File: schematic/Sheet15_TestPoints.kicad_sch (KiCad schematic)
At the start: 16 parts

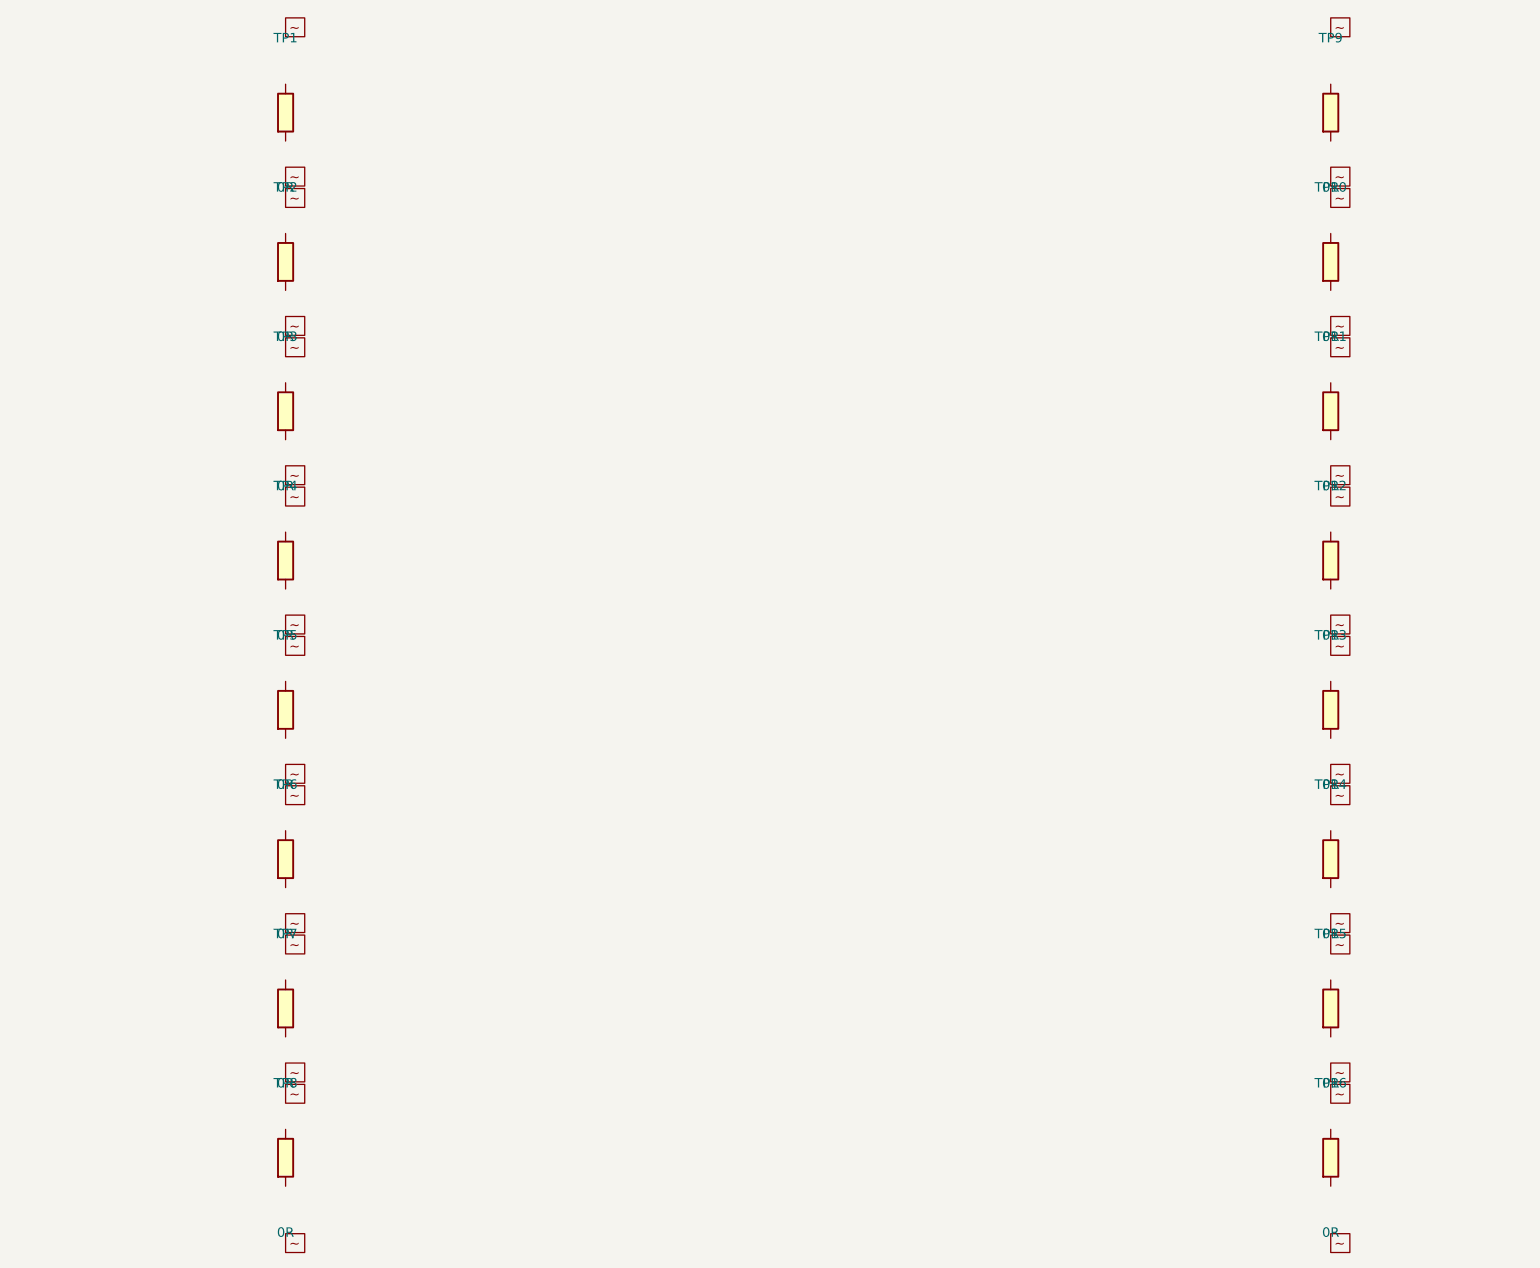
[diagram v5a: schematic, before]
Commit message: feat: connect ALL passive components and fix clock routing
- Added PASSIVE_TOPOLOGY dict mapping 139 passives to their nets
- Passive pin endpoints now get global_labels (was 0 connected, now 138)
- R38 intentionally GND-GND (RECAL_EN pull-down)
- Fixed LMK clock output mapping: CLKout0→ADC_CLK_P, CLKout2→FPGA_REFCLK_P, etc.
- Fixed TPS7H5001-SP SYNC pin collision with LMX_SYNC
- Total connections: 867 pins (up from 641)
- Cross-sheet nets: 52
- Power rails: VIN(33), +3V3(98), GND(228) all with decoupling
- JESD204C: U1↔U2 on 4 lanes ✓
- SPI: U1↔U2↔U3↔U4 ✓
- Clock: LMK→ADC (CLK+SYSREF), LMK→FPGA (REF+SPW) ✓
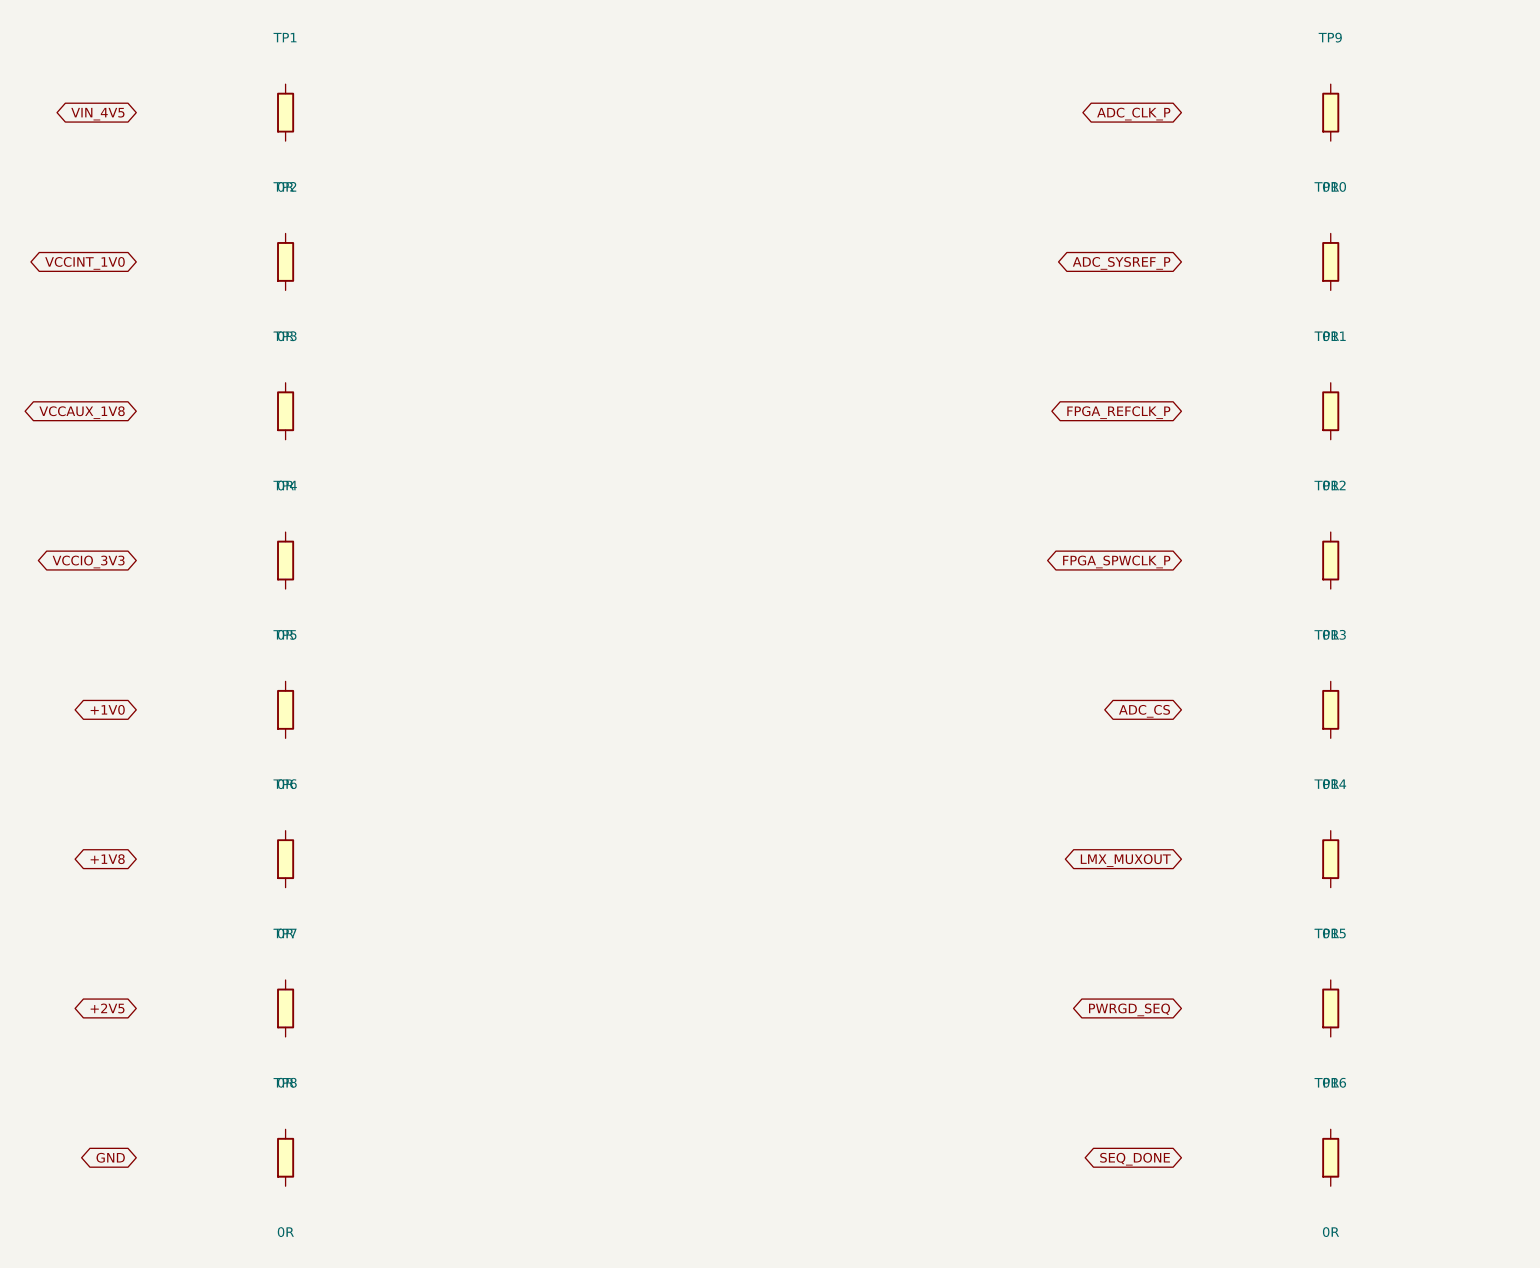
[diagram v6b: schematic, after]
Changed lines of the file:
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@@
     (pin "1")
     (pin "2")
-  )    (symbol (lib_id "Device:R") (at 60 60 0) (unit 1)
+  )  (global_label "VIN_4V5" (shape bidirectional) (at 40 40 180) (effects (font (size 1.27 1.27)) (justify right)))  (symbol (lib_id "Device:R") (at 60 60 0) (unit 1)
     (in_bom yes) (on_board yes)
     (property "Reference" "TP2" (at 60 50 0) (effects (font (size 1.27 1.27))))
@@
     (pin "1")
     (pin "2")
-  )    (symbol (lib_id "Device:R") (at 60 80 0) (unit 1)
+  )  (global_label "VCCINT_1V0" (shape bidirectional) (at 40 60 180) (effects (font (size 1.27 1.27)) (justify right)))  (symbol (lib_id "Device:R") (at 60 80 0) (unit 1)
     (in_bom yes) (on_board yes)
     (property "Reference" "TP3" (at 60 70 0) (effects (font (size 1.27 1.27))))
@@
     (pin "1")
     (pin "2")
-  )    (symbol (lib_id "Device:R") (at 60 100 0) (unit 1)
+  )  (global_label "VCCAUX_1V8" (shape bidirectional) (at 40 80 180) (effects (font (size 1.27 1.27)) (justify right)))  (symbol (lib_id "Device:R") (at 60 100 0) (unit 1)
     (in_bom yes) (on_board yes)
     (property "Reference" "TP4" (at 60 90 0) (effects (font (size 1.27 1.27))))
@@
     (pin "1")
     (pin "2")
-  )    (symbol (lib_id "Device:R") (at 60 120 0) (unit 1)
+  )  (global_label "VCCIO_3V3" (shape bidirectional) (at 40 100 180) (effects (font (size 1.27 1.27)) (justify right)))  (symbol (lib_id "Device:R") (at 60 120 0) (unit 1)
     (in_bom yes) (on_board yes)
     (property "Reference" "TP5" (at 60 110 0) (effects (font (size 1.27 1.27))))
@@
     (pin "1")
     (pin "2")
-  )    (symbol (lib_id "Device:R") (at 60 140 0) (unit 1)
+  )  (global_label "+1V0" (shape bidirectional) (at 40 120 180) (effects (font (size 1.27 1.27)) (justify right)))  (symbol (lib_id "Device:R") (at 60 140 0) (unit 1)
     (in_bom yes) (on_board yes)
     (property "Reference" "TP6" (at 60 130 0) (effects (font (size 1.27 1.27))))
@@
     (pin "1")
     (pin "2")
-  )    (symbol (lib_id "Device:R") (at 60 160 0) (unit 1)
+  )  (global_label "+1V8" (shape bidirectional) (at 40 140 180) (effects (font (size 1.27 1.27)) (justify right)))  (symbol (lib_id "Device:R") (at 60 160 0) (unit 1)
     (in_bom yes) (on_board yes)
     (property "Reference" "TP7" (at 60 150 0) (effects (font (size 1.27 1.27))))
@@
     (pin "1")
     (pin "2")
-  )    (symbol (lib_id "Device:R") (at 60 180 0) (unit 1)
+  )  (global_label "+2V5" (shape bidirectional) (at 40 160 180) (effects (font (size 1.27 1.27)) (justify right)))  (symbol (lib_id "Device:R") (at 60 180 0) (unit 1)
     (in_bom yes) (on_board yes)
     (property "Reference" "TP8" (at 60 170 0) (effects (font (size 1.27 1.27))))
@@
     (pin "1")
     (pin "2")
-  )    (symbol (lib_id "Device:R") (at 200 40 0) (unit 1)
+  )  (global_label "GND" (shape bidirectional) (at 40 180 180) (effects (font (size 1.27 1.27)) (justify right)))  (symbol (lib_id "Device:R") (at 200 40 0) (unit 1)
     (in_bom yes) (on_board yes)
     (property "Reference" "TP9" (at 200 30 0) (effects (font (size 1.27 1.27))))
@@
     (pin "1")
     (pin "2")
-  )    (symbol (lib_id "Device:R") (at 200 60 0) (unit 1)
+  )  (global_label "ADC_CLK_P" (shape bidirectional) (at 180 40 180) (effects (font (size 1.27 1.27)) (justify right)))  (symbol (lib_id "Device:R") (at 200 60 0) (unit 1)
     (in_bom yes) (on_board yes)
     (property "Reference" "TP10" (at 200 50 0) (effects (font (size 1.27 1.27))))
@@
     (pin "1")
     (pin "2")
-  )    (symbol (lib_id "Device:R") (at 200 80 0) (unit 1)
+  )  (global_label "ADC_SYSREF_P" (shape bidirectional) (at 180 60 180) (effects (font (size 1.27 1.27)) (justify right)))  (symbol (lib_id "Device:R") (at 200 80 0) (unit 1)
     (in_bom yes) (on_board yes)
     (property "Reference" "TP11" (at 200 70 0) (effects (font (size 1.27 1.27))))
@@
     (pin "1")
     (pin "2")
-  )    (symbol (lib_id "Device:R") (at 200 100 0) (unit 1)
+  )  (global_label "FPGA_REFCLK_P" (shape bidirectional) (at 180 80 180) (effects (font (size 1.27 1.27)) (justify right)))  (symbol (lib_id "Device:R") (at 200 100 0) (unit 1)
     (in_bom yes) (on_board yes)
     (property "Reference" "TP12" (at 200 90 0) (effects (font (size 1.27 1.27))))
@@
     (pin "1")
     (pin "2")
-  )    (symbol (lib_id "Device:R") (at 200 120 0) (unit 1)
+  )  (global_label "FPGA_SPWCLK_P" (shape bidirectional) (at 180 100 180) (effects (font (size 1.27 1.27)) (justify right)))  (symbol (lib_id "Device:R") (at 200 120 0) (unit 1)
     (in_bom yes) (on_board yes)
     (property "Reference" "TP13" (at 200 110 0) (effects (font (size 1.27 1.27))))
@@
     (pin "1")
     (pin "2")
-  )    (symbol (lib_id "Device:R") (at 200 140 0) (unit 1)
+  )  (global_label "ADC_CS" (shape bidirectional) (at 180 120 180) (effects (font (size 1.27 1.27)) (justify right)))  (symbol (lib_id "Device:R") (at 200 140 0) (unit 1)
     (in_bom yes) (on_board yes)
     (property "Reference" "TP14" (at 200 130 0) (effects (font (size 1.27 1.27))))
@@
     (pin "1")
     (pin "2")
-  )    (symbol (lib_id "Device:R") (at 200 160 0) (unit 1)
+  )  (global_label "LMX_MUXOUT" (shape bidirectional) (at 180 140 180) (effects (font (size 1.27 1.27)) (justify right)))  (symbol (lib_id "Device:R") (at 200 160 0) (unit 1)
     (in_bom yes) (on_board yes)
     (property "Reference" "TP15" (at 200 150 0) (effects (font (size 1.27 1.27))))
@@
     (pin "1")
     (pin "2")
-  )    (symbol (lib_id "Device:R") (at 200 180 0) (unit 1)
+  )  (global_label "PWRGD_SEQ" (shape bidirectional) (at 180 160 180) (effects (font (size 1.27 1.27)) (justify right)))  (symbol (lib_id "Device:R") (at 200 180 0) (unit 1)
     (in_bom yes) (on_board yes)
     (property "Reference" "TP16" (at 200 170 0) (effects (font (size 1.27 1.27))))
@@
     (pin "1")
     (pin "2")
-  )
-  (global_label "~" (at 60.0000 28.5700 0) (effects (font (size 1.27 1.27))))
-  (global_label "~" (at 60.0000 51.4300 0) (effects (font (size 1.27 1.27))))
-  (global_label "~" (at 60.0000 48.5700 0) (effects (font (size 1.27 1.27))))
-  (global_label "~" (at 60.0000 71.4300 0) (effects (font (size 1.27 1.27))))
-  (global_label "~" (at 60.0000 68.5700 0) (effects (font (size 1.27 1.27))))
-  (global_label "~" (at 60.0000 91.4300 0) (effects (font (size 1.27 1.27))))
-  (global_label "~" (at 60.0000 88.5700 0) (effects (font (size 1.27 1.27))))
-  (global_label "~" (at 60.0000 111.4300 0) (effects (font (size 1.27 1.27))))
-  (global_label "~" (at 60.0000 108.5700 0) (effects (font (size 1.27 1.27))))
-  (global_label "~" (at 60.0000 131.4300 0) (effects (font (size 1.27 1.27))))
-  (global_label "~" (at 60.0000 128.5700 0) (effects (font (size 1.27 1.27))))
-  (global_label "~" (at 60.0000 151.4300 0) (effects (font (size 1.27 1.27))))
-  (global_label "~" (at 60.0000 148.5700 0) (effects (font (size 1.27 1.27))))
-  (global_label "~" (at 60.0000 171.4300 0) (effects (font (size 1.27 1.27))))
-  (global_label "~" (at 60.0000 168.5700 0) (effects (font (size 1.27 1.27))))
-  (global_label "~" (at 60.0000 191.4300 0) (effects (font (size 1.27 1.27))))
-  (global_label "~" (at 200.0000 28.5700 0) (effects (font (size 1.27 1.27))))
-  (global_label "~" (at 200.0000 51.4300 0) (effects (font (size 1.27 1.27))))
-  (global_label "~" (at 200.0000 48.5700 0) (effects (font (size 1.27 1.27))))
-  (global_label "~" (at 200.0000 71.4300 0) (effects (font (size 1.27 1.27))))
-  (global_label "~" (at 200.0000 68.5700 0) (effects (font (size 1.27 1.27))))
-  (global_label "~" (at 200.0000 91.4300 0) (effects (font (size 1.27 1.27))))
-  (global_label "~" (at 200.0000 88.5700 0) (effects (font (size 1.27 1.27))))
-  (global_label "~" (at 200.0000 111.4300 0) (effects (font (size 1.27 1.27))))
-  (global_label "~" (at 200.0000 108.5700 0) (effects (font (size 1.27 1.27))))
-  (global_label "~" (at 200.0000 131.4300 0) (effects (font (size 1.27 1.27))))
-  (global_label "~" (at 200.0000 128.5700 0) (effects (font (size 1.27 1.27))))
-  (global_label "~" (at 200.0000 151.4300 0) (effects (font (size 1.27 1.27))))
-  (global_label "~" (at 200.0000 148.5700 0) (effects (font (size 1.27 1.27))))
-  (global_label "~" (at 200.0000 171.4300 0) (effects (font (size 1.27 1.27))))
-  (global_label "~" (at 200.0000 168.5700 0) (effects (font (size 1.27 1.27))))
-  (global_label "~" (at 200.0000 191.4300 0) (effects (font (size 1.27 1.27))))
-  (sheet_instances (path "/" (page "1")))
+  )  (global_label "SEQ_DONE" (shape bidirectional) (at 180 180 180) (effects (font (size 1.27 1.27)) (justify right)))  (sheet_instances (path "/" (page "1")))
 )
